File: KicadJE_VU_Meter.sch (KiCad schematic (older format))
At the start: 67 parts, among them J1 Out1, J2 Out2, J3 In1.1, J5 In1.3, P1 HEADER_2x5_Doepfer, U1 TL072, U2 TL072

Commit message: Footprint updates
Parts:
- P1: footprint Connector_IDC:IDC-Header_2x05_P2.54mm_Vertical -> Connector_PinHeader_2.54mm:PinHeader_2x05_P2.54mm_Vertical_SMD
- U1, U2: footprint AJ-Dropbox-Kicad:AJ_SO-8_5.3x6.2mm_P1.27mm -> Package_SO:SO-8_5.3x6.2mm_P1.27mm
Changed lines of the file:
@@
 F 0 "U1" V 2675 1125 50  0000 C CNN
 F 1 "TL072" V 2675 1650 50  0000 C CNN
-F 2 "AJ-Dropbox-Kicad:AJ_SO-8_5.3x6.2mm_P1.27mm" H 2825 1400 50  0001 C CNN
+F 2 "Package_SO:SO-8_5.3x6.2mm_P1.27mm" H 2825 1400 50  0001 C CNN
 F 3 "http://www.ti.com/lit/ds/symlink/tl071.pdf" H 2825 1400 50  0001 C CNN
 	3    2825 1400
@@
 F 0 "P1" H 1875 902 40  0000 C CNN
 F 1 "HEADER_2x5_Doepfer" H 1850 1100 40  0000 C CNN
-F 2 "Connector_IDC:IDC-Header_2x05_P2.54mm_Vertical" H 1525 650 60  0000 C CNN
+F 2 "Connector_PinHeader_2.54mm:PinHeader_2x05_P2.54mm_Vertical_SMD" H 1525 650 60  0000 C CNN
 F 3 "" H 1875 1400 60  0000 C CNN
 	1    1875 1400
@@
 F 0 "U2" H 2325 7450 50  0000 C CNN
 F 1 "TL072" H 2275 7525 50  0000 C CNN
-F 2 "AJ-Dropbox-Kicad:AJ_SO-8_5.3x6.2mm_P1.27mm" H 2300 7475 50  0001 C CNN
+F 2 "Package_SO:SO-8_5.3x6.2mm_P1.27mm" H 2300 7475 50  0001 C CNN
 F 3 "http://www.ti.com/lit/ds/symlink/tl071.pdf" H 2300 7475 50  0001 C CNN
 	2    2300 7475
@@
 F 0 "U2" V 2800 1125 50  0000 C CNN
 F 1 "TL072" V 2800 1650 50  0000 C CNN
-F 2 "AJ-Dropbox-Kicad:AJ_SO-8_5.3x6.2mm_P1.27mm" H 2950 1400 50  0001 C CNN
+F 2 "Package_SO:SO-8_5.3x6.2mm_P1.27mm" H 2950 1400 50  0001 C CNN
 F 3 "http://www.ti.com/lit/ds/symlink/tl071.pdf" H 2950 1400 50  0001 C CNN
 	3    2950 1400
@@
 F 0 "U2" H 6325 5225 50  0000 C CNN
 F 1 "TL072" H 6525 5075 50  0000 C CNN
-F 2 "AJ-Dropbox-Kicad:AJ_SO-8_5.3x6.2mm_P1.27mm" H 6425 5225 50  0001 C CNN
+F 2 "Package_SO:SO-8_5.3x6.2mm_P1.27mm" H 6425 5225 50  0001 C CNN
 F 3 "http://www.ti.com/lit/ds/symlink/tl071.pdf" H 6425 5225 50  0001 C CNN
 	1    6425 5225
@@
 F 0 "U1" H 5800 1650 50  0000 C CNN
 F 1 "TL072" H 5800 1550 50  0000 C CNN
-F 2 "AJ-Dropbox-Kicad:AJ_SO-8_5.3x6.2mm_P1.27mm" H 5875 1600 50  0001 C CNN
+F 2 "Package_SO:SO-8_5.3x6.2mm_P1.27mm" H 5875 1600 50  0001 C CNN
 F 3 "http://www.ti.com/lit/ds/symlink/tl071.pdf" H 5875 1600 50  0001 C CNN
 	1    5875 1600
@@
 F 0 "U1" H 5800 2900 50  0000 C CNN
 F 1 "TL072" H 5800 2800 50  0000 C CNN
-F 2 "AJ-Dropbox-Kicad:AJ_SO-8_5.3x6.2mm_P1.27mm" H 5875 2850 50  0001 C CNN
+F 2 "Package_SO:SO-8_5.3x6.2mm_P1.27mm" H 5875 2850 50  0001 C CNN
 F 3 "http://www.ti.com/lit/ds/symlink/tl071.pdf" H 5875 2850 50  0001 C CNN
 	2    5875 2850

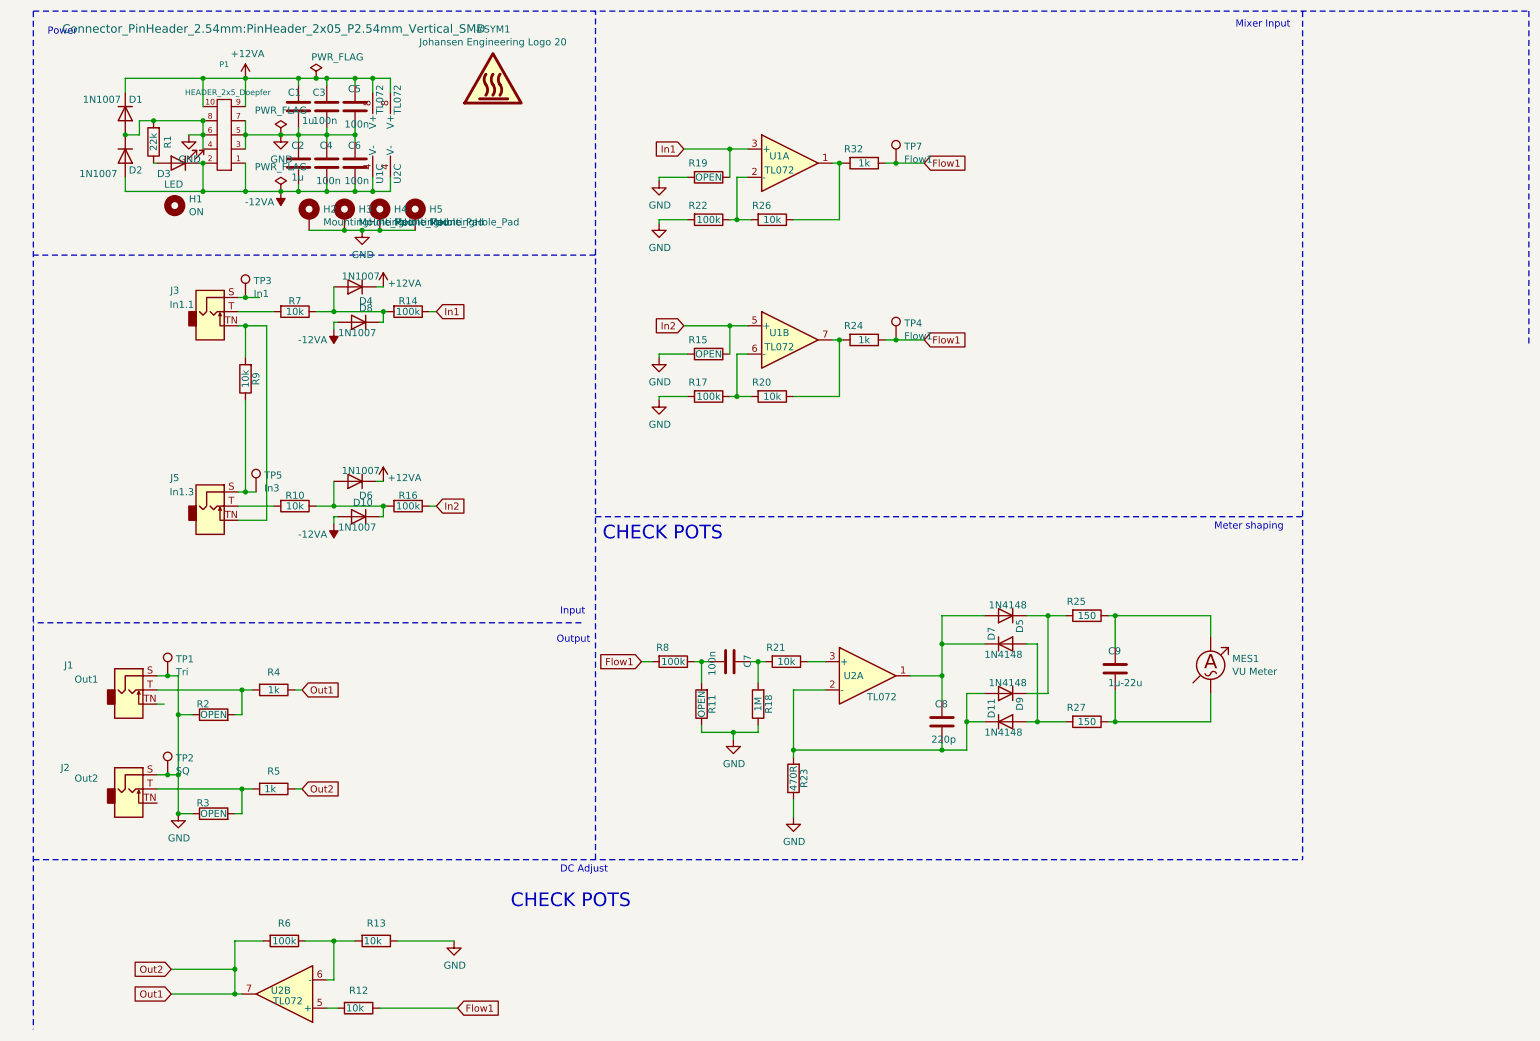
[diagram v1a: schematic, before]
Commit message: Update KicadJE_VU_Meter.sch
update resistors and capacitors footprints
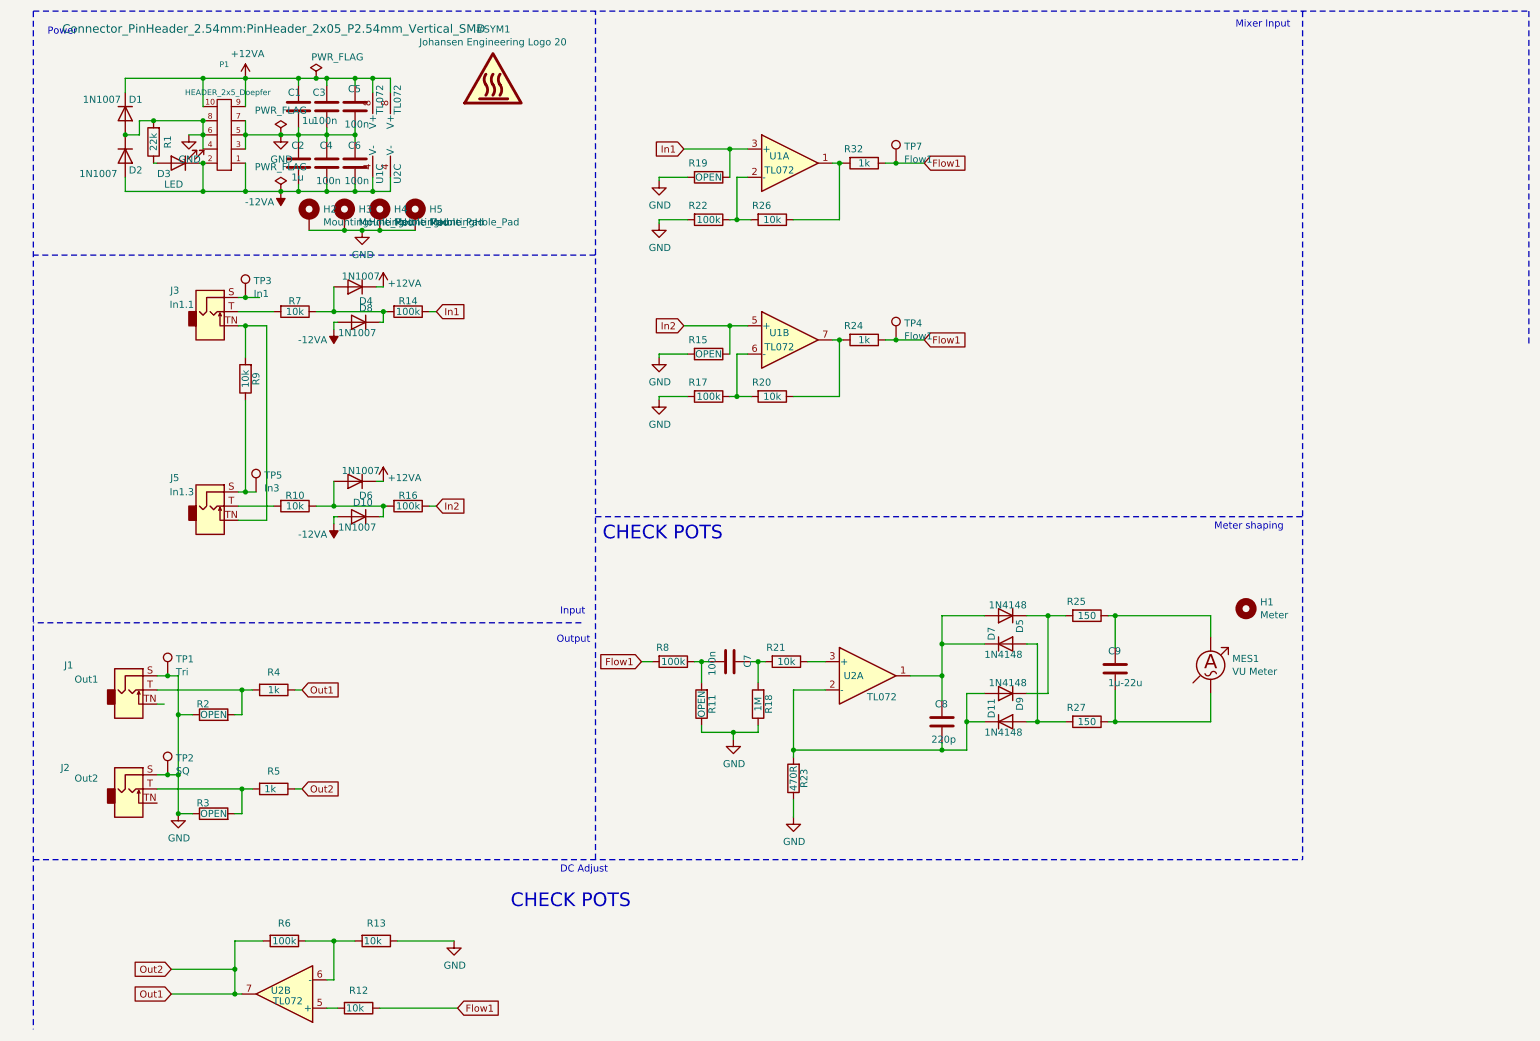
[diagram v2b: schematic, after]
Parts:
- C1, C2: footprint Capacitor_SMD:C_1206_3216Metric_Pad1.42x1.75mm_HandSolder -> Capacitor_SMD:C_0805_2012Metric
- C3, C4, C5, C6, C7, C8: footprint Capacitor_SMD:C_0805_2012Metric_Pad1.15x1.40mm_HandSolder -> Capacitor_SMD:C_0805_2012Metric
- C9: footprint Capacitor_SMD:C_1206_3216Metric_Pad1.42x1.75mm_HandSolder -> Capacitor_SMD:C_1206_3216Metric
- H1: value ON -> Meter; footprint AJ:LED_Hole_3mm -> MountingHole:MountingHole_8.4mm_M8_Pad_Via
- R1, R10, R11, R12, R13, R14, R15, R16, R17, R18, R19, R2, R20, R21, R22, R23, R24, R25, R26, R27, R3, R32, R4, R5, R6, R7, R8, R9: footprint Resistor_SMD:R_0805_2012Metric_Pad1.15x1.40mm_HandSolder -> Resistor_SMD:R_0805_2012Metric_Pad1.20x1.40mm_HandSolder
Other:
- moved on the sheet: H1

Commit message: Footprint and faceplate cleanup
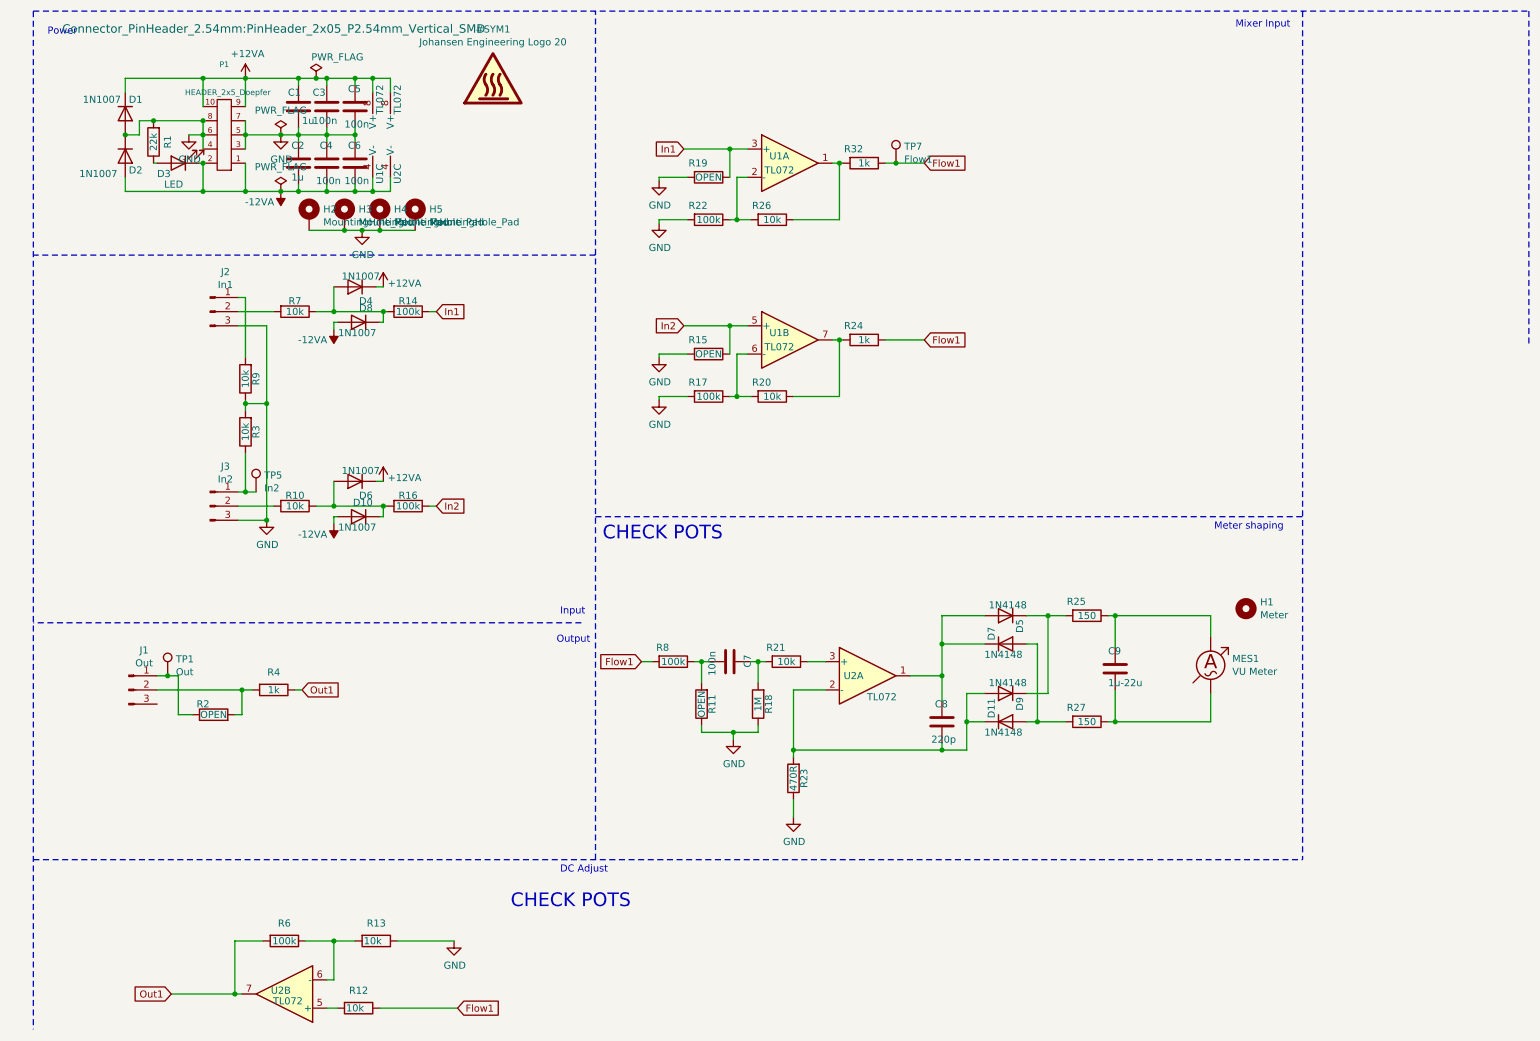
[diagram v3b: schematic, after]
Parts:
- removed J1: Out1, Connector_PinHeader_2.54mm:PinHeader_1x03_P2.54mm_Vertical_SMD_Pin1Right, symbol Connector:AudioJack2_SwitchT
- removed J2: Out2, Connector_PinHeader_2.54mm:PinHeader_1x03_P2.54mm_Vertical_SMD_Pin1Right, symbol Connector:AudioJack2_SwitchT
- removed J3: In1.1, Connector_PinHeader_2.54mm:PinHeader_1x03_P2.54mm_Vertical_SMD_Pin1Right, symbol Connector:AudioJack2_SwitchT
- removed J5: In1.3, Connector_PinHeader_2.54mm:PinHeader_1x03_P2.54mm_Vertical_SMD_Pin1Right, symbol Connector:AudioJack2_SwitchT
- removed R5: 1k, Resistor_SMD:R_0805_2012Metric_Pad1.20x1.40mm_HandSolder, symbol Device:R
- removed TP2: SQ, AJ:Jack_6m3, symbol Connector:TestPoint
- removed TP3: In1, AJ:Jack_6m3, symbol Connector:TestPoint
- removed TP4: Flow1, AJ:Pot_6m3_scale1, symbol Connector:TestPoint
- added J1: Out, Connector_PinHeader_2.54mm:PinHeader_1x03_P2.54mm_Vertical_SMD_Pin1Right, symbol Connector:Conn_01x03_Male
- added J2: In1, Connector_PinHeader_2.54mm:PinHeader_1x03_P2.54mm_Vertical_SMD_Pin1Right, symbol Connector:Conn_01x03_Male
- added J3: In2, Connector_PinHeader_2.54mm:PinHeader_1x03_P2.54mm_Vertical_SMD_Pin1Right, symbol Connector:Conn_01x03_Male
- H1: footprint MountingHole:MountingHole_8.4mm_M8_Pad_Via -> AJ:VU_Meter_Hole
- R3: value OPEN -> 10k
- TP1: value Tri -> Out; footprint AJ:Jack_6m3 -> TestPoint:TestPoint_Pad_D2.0mm
- TP5: value In3 -> In2; footprint AJ:Jack_6m3 -> TestPoint:TestPoint_Pad_D2.0mm
- TP7: footprint AJ:Pot_6m3_scale1 -> TestPoint:TestPoint_Pad_D2.0mm
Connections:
- net GND: now also R3.2, R9.1, J2.3 (Pin_3), J3.3 (Pin_3); no longer R2.1, R3.1, TP1.1
- net at R2.2, R4.2: now also J1.2 (Pin_2)
- net at TP5.1: now also R3.1, J3.1 (Pin_1); no longer R9.1
- net at R9.2: now also J2.1 (Pin_1)
- net at R7.2: now also J2.2 (Pin_2)
- net at R10.2: now also J3.2 (Pin_2)
- new net: J1.1 (Pin_1), R2.1, TP1.1

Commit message: Update KicadJE_VU_Meter.sch
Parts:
- D10: renamed from D9; footprint Diode_SMD:D_MiniMELF_Handsoldering -> Diode_SMD:D_MiniMELF
- D11: footprint Diode_SMD:D_MiniMELF_Handsoldering -> Diode_SMD:D_MiniMELF
- D8: renamed from D5; footprint Diode_SMD:D_MiniMELF_Handsoldering -> Diode_SMD:D_MiniMELF
- D9: renamed from D7; footprint Diode_SMD:D_MiniMELF_Handsoldering -> Diode_SMD:D_MiniMELF
- renumbered D6 to D5, D8 to D6, D10 to D7, H2 to H1, H3 to H2, H4 to H3, H5 to H4, H1 to H5, R13 to R10, R14 to R11, R16 to R12, R8 to R13, R11 to R14, R19 to R15, R22 to R16, R15 to R17, R17 to R18, R18 to R19, R26 to R20, R20 to R21, R21 to R22, R32 to R24, R24 to R25, R25 to R26, R9 to R3, R3 to R4, R4 to R5, R10 to R8, R12 to R9, TP5 to TP2, TP7 to TP3, U2 to U1, U1 to U2
